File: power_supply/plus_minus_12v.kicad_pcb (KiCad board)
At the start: 2 copper layers, 35 parts, among them P1 CONN_01X03, P2 CONN_01X03, T1 MYRRA-TRANSF, U1 LM317T, U2 LM337T

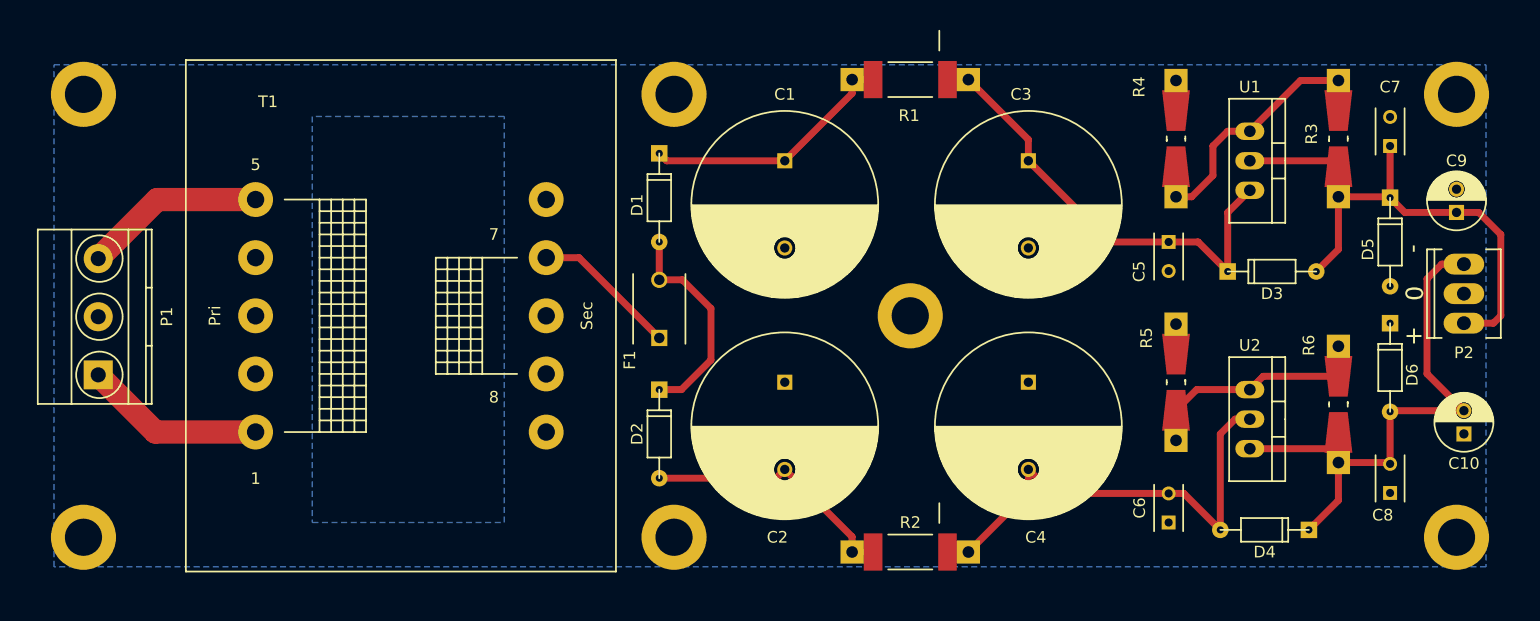
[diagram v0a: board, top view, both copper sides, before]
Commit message: New transformer footprint, updated power PCB
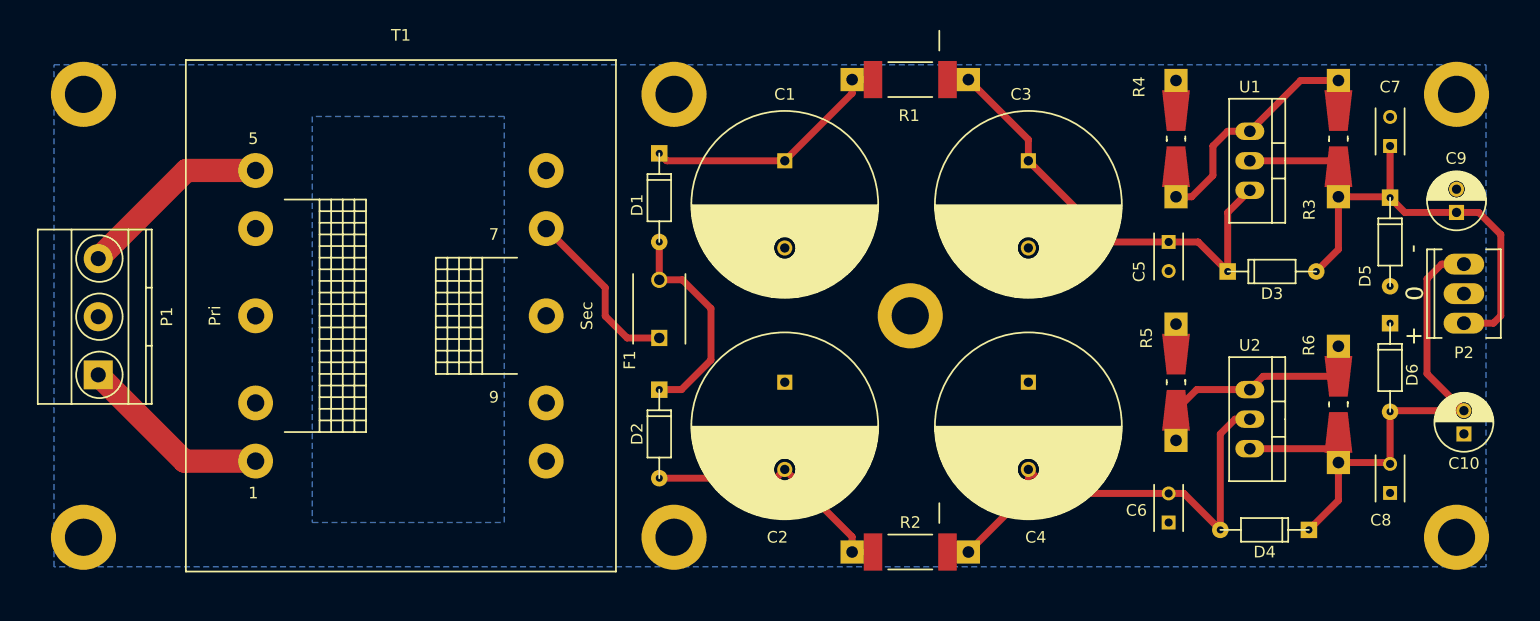
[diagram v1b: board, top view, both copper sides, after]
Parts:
- T1: footprint Transformers_CHK:Trafo_CHK-EI42-5VA_1xSec -> My Shit:Transformer-5VA_1xSec
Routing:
- net Net-(F1-Pad1): track 12.6 -> 15.1 mm
- net Net-(P1-Pad3): track 15.6 -> 16.7 mm
- net Net-(P1-Pad1): track 15.6 -> 16.6 mm

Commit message: Adding a CUT OUT text for Osh Park
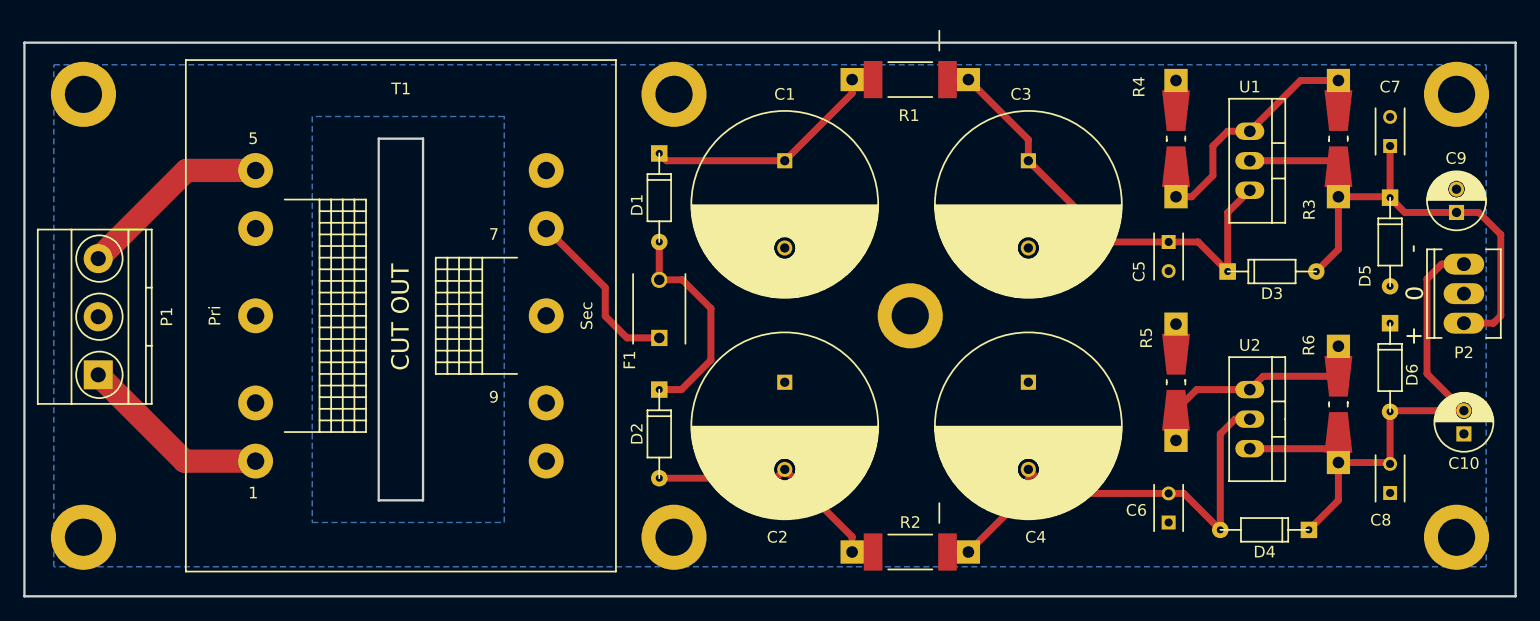
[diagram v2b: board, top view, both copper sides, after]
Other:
- board outline added: 128.3 x 47.6 mm
- board text added: "(C) Jon Ronen-Drori 2016"
- board text added: "CUT OUT"
- board text added: "https://oshpark.com/profiles/jronen"
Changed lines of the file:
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@@
     (links 68)
     (no_connects 0)
-    (area 47.650714 79.505 196.189286 130.135)
+    (area 47.650714 79.813839 196.189286 130.135)
     (thickness 1.6)
-    (drawings 11)
+    (drawings 14)
     (tracks 89)
     (zones 0)
@@
     (trace_min 0.4)
     (segment_width 0.2)
-    (edge_width 0.15)
+    (edge_width 0.2)
     (via_size 0.8)
     (via_drill 0.5)
@@
     (descr "Trafo, Printtrafo, CHK, EI42, 5VA, 1x Sec,")
     (tags "Trafo, Printtrafo, CHK, EI42, 5VA, 1x Sec,")
-    (fp_text reference T1 (at 0 -24.13) (layer F.SilkS)
-      (effects (font (size 1 1) (thickness 0.15)))
-    )
-    (fp_text value MYRRA-TRANSF (at 0 0 90) (layer F.Fab)
+    (fp_text reference T1 (at 0.0254 -19.5199) (layer F.SilkS)
+      (effects (font (size 1 1) (thickness 0.15)))
+    )
+    (fp_text value MYRRA-TRANSF (at 0 0 90) (layer F.Fab) hide
       (effects (font (size 1 1) (thickness 0.15)))
     )
@@
     (pad 10 thru_hole circle (at 12.49934 12.5) (size 2.99974 2.99974) (drill 1.50114) (layers *.Cu *.Mask F.SilkS))
   )
+  (gr_text https://oshpark.com/profiles/jronen (at 132.4737 115.0366) (layer B.SilkS)
+    (effects (font (size 1.5 1.5) (thickness 0.3)) (justify mirror))
+  )
+  (gr_text "(C) Jon Ronen-Drori 2016" (at 133.6802 96.1009) (layer B.SilkS)
+    (effects (font (size 1.5 1.5) (thickness 0.3)) (justify mirror))
+  )
+  (gr_text "CUT OUT" (at 90.1446 105.5243 90) (layer F.SilkS)
+    (effects (font (size 1.5 1.5) (thickness 0.3)))
+  )
   (gr_text + (at 177.3174 107.0991) (layer F.SilkS)
     (effects (font (size 1.5 1.5) (thickness 0.3)))
@@
     (effects (font (size 1.5 1.5) (thickness 0.3)))
   )
-  (gr_line (start 88.265 90.17) (end 92.075 90.17) (angle 90) (layer Margin) (width 0.2))
-  (gr_line (start 88.265 121.285) (end 92.075 121.285) (angle 90) (layer Margin) (width 0.2))
-  (gr_line (start 57.785 129.54) (end 57.785 81.915) (angle 90) (layer Margin) (width 0.2))
-  (gr_line (start 186.055 129.54) (end 57.785 129.54) (angle 90) (layer Margin) (width 0.2))
-  (gr_line (start 186.055 81.915) (end 186.055 129.54) (angle 90) (layer Margin) (width 0.2))
-  (gr_line (start 57.785 81.915) (end 186.055 81.915) (angle 90) (layer Margin) (width 0.2))
-  (gr_line (start 92.075 90.17) (end 92.075 121.285) (angle 90) (layer Margin) (width 0.2))
-  (gr_line (start 88.265 121.285) (end 88.265 90.17) (angle 90) (layer Margin) (width 0.2))
+  (gr_line (start 88.265 90.17) (end 92.075 90.17) (angle 90) (layer Edge.Cuts) (width 0.2))
+  (gr_line (start 88.265 121.285) (end 92.075 121.285) (angle 90) (layer Edge.Cuts) (width 0.2))
+  (gr_line (start 57.785 129.54) (end 57.785 81.915) (angle 90) (layer Edge.Cuts) (width 0.2))
+  (gr_line (start 186.055 129.54) (end 57.785 129.54) (angle 90) (layer Edge.Cuts) (width 0.2))
+  (gr_line (start 186.055 81.915) (end 186.055 129.54) (angle 90) (layer Edge.Cuts) (width 0.2))
+  (gr_line (start 57.785 81.915) (end 186.055 81.915) (angle 90) (layer Edge.Cuts) (width 0.2))
+  (gr_line (start 92.075 90.17) (end 92.075 121.285) (angle 90) (layer Edge.Cuts) (width 0.2))
+  (gr_line (start 88.265 121.285) (end 88.265 90.17) (angle 90) (layer Edge.Cuts) (width 0.2))
   (segment (start 123.19 92.075) (end 113.03 92.075) (width 0.6) (layer F.Cu) (net 1))
   (segment (start 113.03 92.075) (end 112.395 91.44) (width 0.6) (layer F.Cu) (net 1))
